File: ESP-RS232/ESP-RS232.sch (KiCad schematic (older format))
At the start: 3 parts

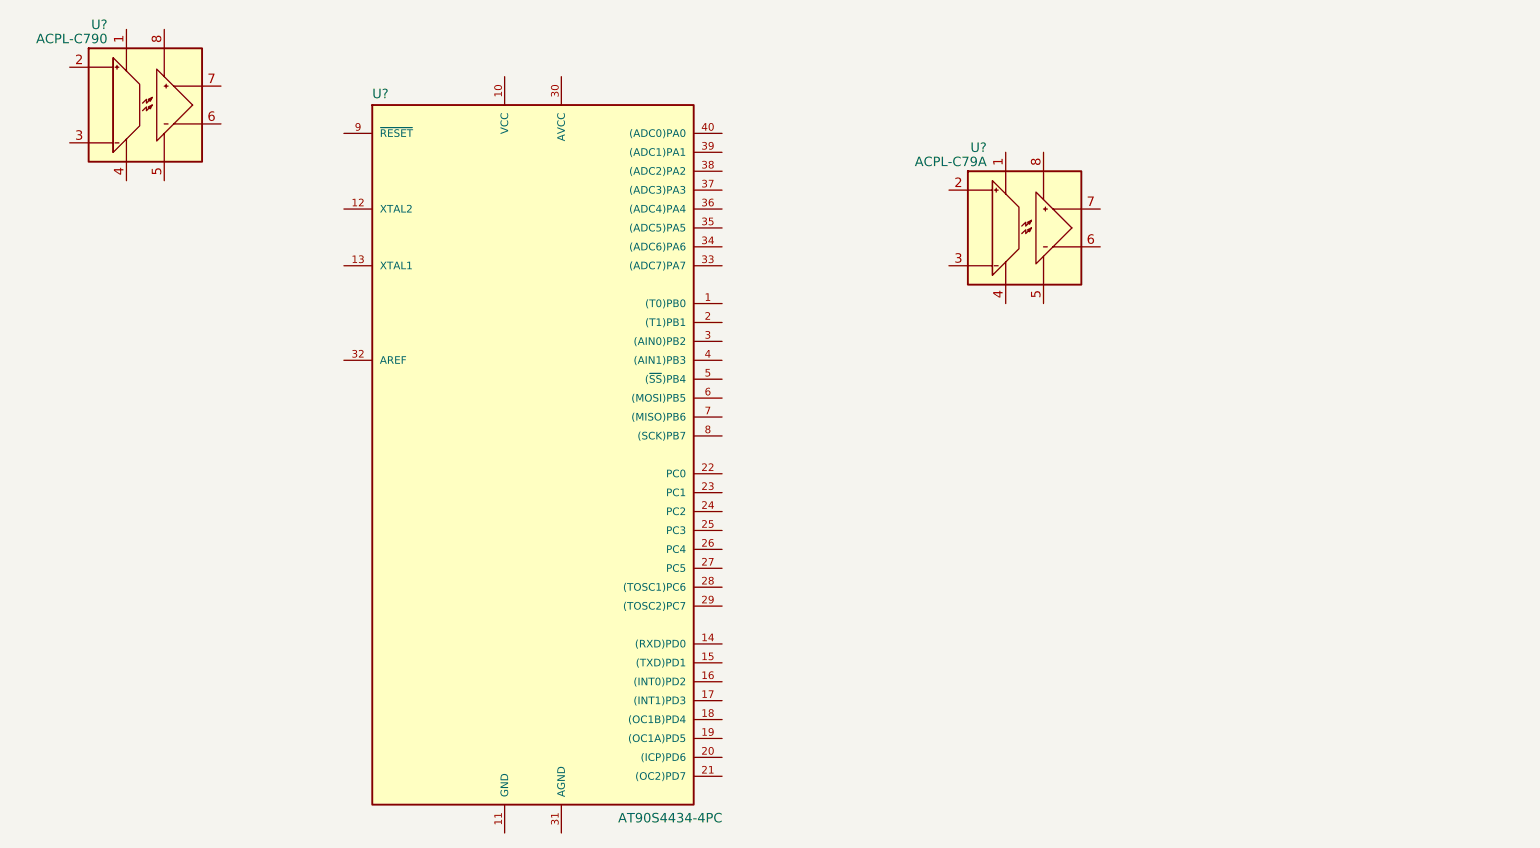
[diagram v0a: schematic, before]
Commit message: First draft of ESP-RS232 tool
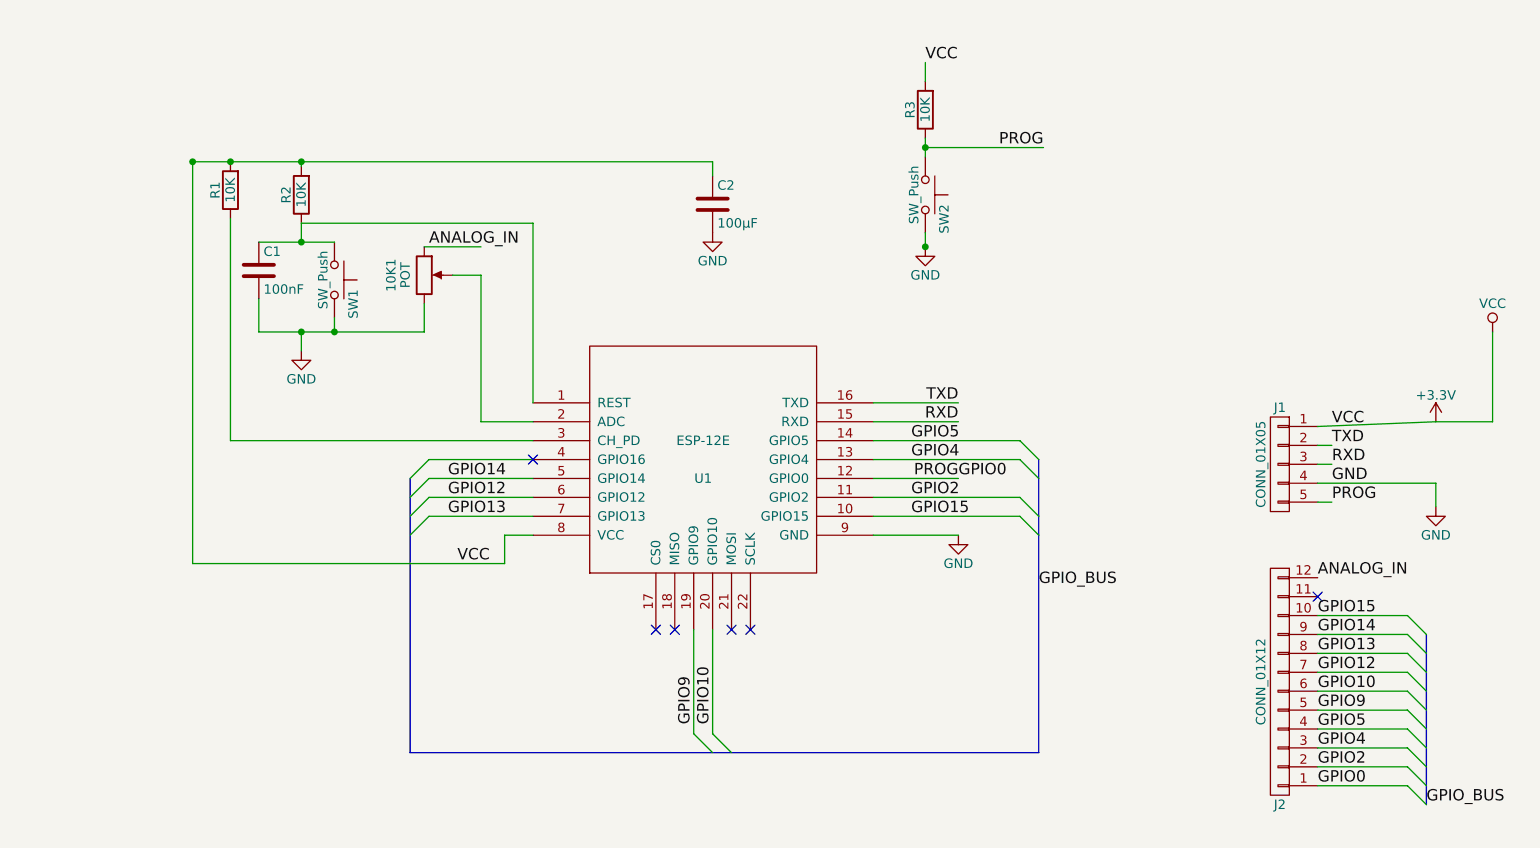
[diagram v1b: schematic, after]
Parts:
- removed U?: ACPL-C790, Housings_SOIC:SOIC-8_5.850x6.807mm_Pitch1.27mm, symbol ACPL-C790
- removed U?: AT90S4434-4PC, DIL40, symbol AT90S4434-4PC
- removed U?: ACPL-C79A, Housings_SOIC:SOIC-8_5.850x6.807mm_Pitch1.27mm, symbol ACPL-C79A
- added 10K1: POT, symbol POT
- added C1: 100nF, symbol C
- added C2: 100µF, symbol C
- added J1: CONN_01X05, symbol CONN_01X05
- added J2: CONN_01X12, symbol CONN_01X12
- added R1, R2, R3: 10K, symbol R
- added SW1, SW2: SW_Push, symbol SW_Push
- added U1: ESP-12E, symbol ESP-12E
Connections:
- new net: C1.1, R2.1, SW1.1, U1.1 (REST)
- new net: 10K1.2, U1.2 (ADC)
- new net: R1.1, U1.3 (CH_PD)
- new net +3V3: C2.1, J1.1 (P1), R1.2, R2.2, R3.2, U1.8 (VCC)
- new net ANALOG_IN: 10K1.1, J2.12 (P12)
- new net GND: 10K1.3, C1.2, C2.2, J1.4 (P4), SW1.2, SW2.2, U1.9 (GND)
- new net GPIO0: J1.5 (P5), J2.1 (P1), R3.1, SW2.1, U1.12 (GPIO0)
- new net GPIO10: J2.6 (P6), U1.20 (GPIO10)
- new net GPIO12: J2.7 (P7), U1.6 (GPIO12)
- new net GPIO13: J2.8 (P8), U1.7 (GPIO13)
- new net GPIO14: J2.9 (P9), U1.5 (GPIO14)
- new net GPIO15: J2.10 (P10), U1.10 (GPIO15)
- new net GPIO2: J2.2 (P2), U1.11 (GPIO2)
- new net GPIO4: J2.3 (P3), U1.13 (GPIO4)
- new net GPIO5: J2.4 (P4), U1.14 (GPIO5)
- new net GPIO9: J2.5 (P5), U1.19 (GPIO9)
- new net RXD: J1.3 (P3), U1.15 (RXD)
- new net TXD: J1.2 (P2), U1.16 (TXD)
- no-connect marks 0 -> 6

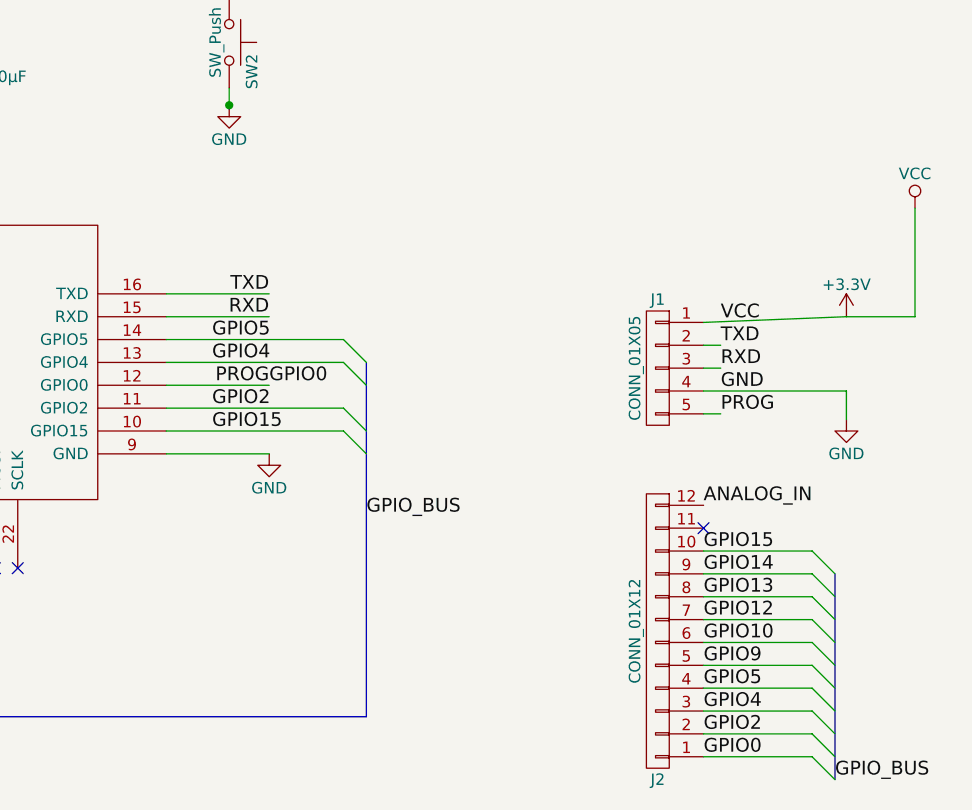
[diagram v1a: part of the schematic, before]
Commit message: fixed ERC with power outlets
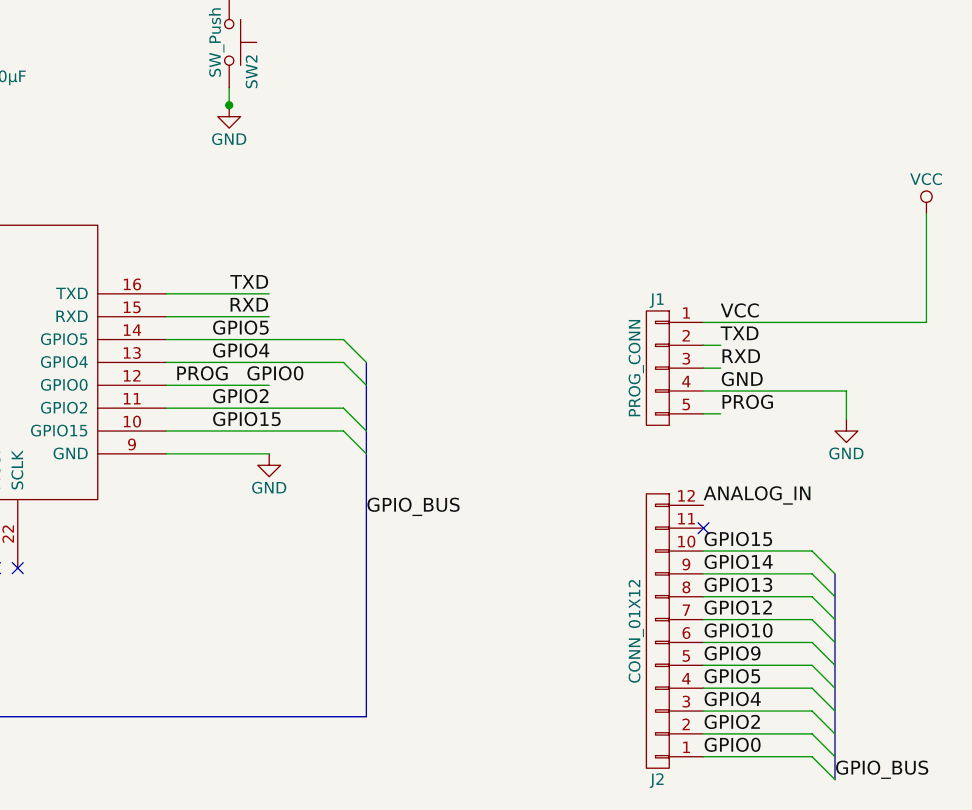
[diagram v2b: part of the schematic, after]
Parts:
- removed J1: CONN_01X05, symbol CONN_01X05
- added J1: PROG_CONN, symbol PROG_CONN
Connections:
- net GND: now also J1.4 (P4)
- net GPIO0: now also J1.5 (P5)
- net RXD: now also J1.3 (P3)
- net TXD: now also J1.2 (P2)
- net +3V3 renamed VCC
- net VCC: now also J1.1 (P1)
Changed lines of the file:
@@
 LIBS:ESP8266
 LIBS:switches
+LIBS:ESP-RS232
 LIBS:ESP-RS232-cache
 EELAYER 25 0
@@
 	1    0    0    -1
 $EndComp
-$Comp
-L CONN_01X05 J1
-U 1 1 58DBCCC4
-P 7550 3350
-F 0 "J1" H 7550 3650 50  0000 C CNN
-F 1 "CONN_01X05" V 7650 3350 50  0000 C CNN
-F 2 "" H 7550 3350 50  0001 C CNN
-F 3 "" H 7550 3350 50  0001 C CNN
-	1    7550 3350
-	-1   0    0    -1
-$EndComp
 Text Label 7825 3150 0    60   ~ 0
 VCC
@@
 Text Label 7825 3550 0    60   ~ 0
 PROG
-Text Label 5850 3425 2    60   ~ 0
+Text Label 5675 3425 2    60   ~ 0
 PROG
 Text Label 5850 3125 2    60   ~ 0
@@
 Connection ~ 2000 1750
 Wire Bus Line
-	6275 3325 6275 4875
+	6275 4875 6275 3325
 Wire Wire Line
 	5400 3225 6175 3225
@@
 	5400 3625 6175 3625
 Wire Wire Line
-	7750 3150 8375 3125
+	7750 3150 8725 3150
 Wire Wire Line
 	7750 3250 7825 3250
@@
 GPIO_BUS
 $Comp
-L +3.3V #PWR05
-U 1 1 58DCE90C
-P 8375 3125
-F 0 "#PWR05" H 8375 2975 50  0001 C CNN
-F 1 "+3.3V" H 8375 3265 50  0000 C CNN
-F 2 "" H 8375 3125 50  0001 C CNN
-F 3 "" H 8375 3125 50  0001 C CNN
-	1    8375 3125
-	1    0    0    -1
-$EndComp
-$Comp
-L VCC #PWR06
+L VCC #PWR05
 U 1 1 58DCE941
-P 8675 2650
-F 0 "#PWR06" H 8675 2500 50  0001 C CNN
-F 1 "VCC" H 8675 2800 50  0000 C CNN
-F 2 "" H 8675 2650 50  0001 C CNN
-F 3 "" H 8675 2650 50  0001 C CNN
-	1    8675 2650
-	1    0    0    -1
-$EndComp
-Wire Wire Line
-	8375 3125 8675 3125
-Wire Wire Line
-	8675 3125 8675 2650
-Text Label 5850 3425 0    60   ~ 0
+P 8725 2675
+F 0 "#PWR05" H 8725 2525 50  0001 C CNN
+F 1 "VCC" H 8725 2825 50  0000 C CNN
+F 2 "" H 8725 2675 50  0001 C CNN
+F 3 "" H 8725 2675 50  0001 C CNN
+	1    8725 2675
+	1    0    0    -1
+$EndComp
+Wire Wire Line
+	8725 3150 8725 2675
+Text Label 5750 3425 0    60   ~ 0
 GPIO0
 Text Label 5600 3525 0    60   ~ 0
@@
 GPIO15
 $Comp
-L GND #PWR07
+L GND #PWR06
 U 1 1 58DCF2D0
 P 5850 3725
-F 0 "#PWR07" H 5850 3475 50  0001 C CNN
+F 0 "#PWR06" H 5850 3475 50  0001 C CNN
 F 1 "GND" H 5850 3575 50  0000 C CNN
 F 2 "" H 5850 3725 50  0001 C CNN
@@
 NoConn ~ 4250 4225
 NoConn ~ 7750 4050
+$Comp
+L PROG_CONN J1
+U 1 1 58DD124D
+P 7550 3350
+F 0 "J1" H 7550 3650 50  0000 C CNN
+F 1 "PROG_CONN" V 7650 3350 50  0000 C CNN
+F 2 "" H 7550 3350 50  0001 C CNN
+F 3 "" H 7550 3350 50  0001 C CNN
+	1    7550 3350
+	-1   0    0    -1
+$EndComp
 $EndSCHEMATC
